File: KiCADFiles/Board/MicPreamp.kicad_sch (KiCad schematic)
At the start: 13 parts, among them U302B2 OPA2348, U6 THAT151xx08

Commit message: chose all components
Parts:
- removed C22: 3300u, ~, symbol PCM_SparkFun-Capacitor:C_Polarized_Small
- removed U302B2: OPA2348, symbol SuperAudioBoard-rescue:OPA2348
- added U10: OPA1655D, Package_SO:SOIC-8_3.9x4.9mm_P1.27mm, symbol Amplifier_Operational:OPA1655D
- C24, C39: value 470pF -> 470p; MPN (none) -> C0603C471J5GACTU
- C40: value 0.1uF -> 0.1u; MPN (none) -> CL10B104KB8NNNL
- R10: footprint (none) -> PCM_SparkFun-Resistor:R_0805_2012Metric; MPN (none) -> RC0805FR-074R7L
- R11, R17: footprint (none) -> PCM_SparkFun-Resistor:R_0805_2012Metric; MPN (none) -> ERA-6AEB102V
- R16, R7: footprint (none) -> PCM_SparkFun-Resistor:R_0805_2012Metric; MPN (none) -> ERA-6AEB3922V
- R6: value 10 -> 34; footprint ~ -> PCM_SparkFun-Resistor:R_0805_2012Metric; MPN (none) -> CRCW080534R0FKEA
- RV3: value RD_10k -> 5k; footprint (none) -> Potentiometer_THT:Potentiometer_Alps_RK163_Single_Horizontal; MPN (none) -> RV16AF-10-15K-C5K-3LA; now not fitted
- U6: value THAT151xx08 -> 1512S08-U; footprint (none) -> Package_SO:SOIC-8_5.3x5.3mm_P1.27mm; MPN (none) -> 1512S08-U
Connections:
- net +15V: now also U10.7 (V+)
- net GND: now also U10.4 (V-)
- net Rg-: now also RV3.3
- net at R6.1: now also U10.2 (-), U10.6
- net at R16.2, R7.1: now also U10.3 (+)
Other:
- moved on the sheet: R10

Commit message: replaced sw with relay, routed line amp section
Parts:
- added C22: 0.1u, PCM_SparkFun-Capacitor:C_0603_1608Metric, symbol PCM_SparkFun-Capacitor:0.1uF_0603_25V_20%
- C24, C39: footprint PCM_SparkFun-Capacitor:C_0603_1608Metric -> PCM_SparkFun-Capacitor:C_0805_2012Metric; MPN C0603C471J5GACTU -> 08053C471KAT2A
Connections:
- net +15V: now also C22.2
- net GND: now also C22.1
- net Rg-: now also RV3.2
- net at R10.2, RV3.1: no longer RV3.2
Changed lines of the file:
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@@
-	)
-	(junction
-		(at 160.02 114.3)
-		(diameter 0)
-		(color 0 0 0 0)
 	)
 	(junction
@@
 	)
 	(junction
+		(at 160.02 121.92)
+		(diameter 0)
+		(color 0 0 0 0)
+	)
+	(junction
 		(at 156.21 74.93)
+		(diameter 0)
+		(color 0 0 0 0)
+	)
+	(junction
+		(at 59.69 57.15)
 		(diameter 0)
 		(color 0 0 0 0)
@@
 	(wire
 		(pts
+			(xy 53.34 57.15) (xy 59.69 57.15)
+		)
+		(stroke
+			(width 0)
+			(type default)
+		)
+	)
+	(wire
+		(pts
 			(xy 199.39 72.39) (xy 198.12 72.39)
 		)
@@
 	(wire
 		(pts
+			(xy 163.83 121.92) (xy 160.02 121.92)
+		)
+		(stroke
+			(width 0)
+			(type default)
+		)
+	)
+	(wire
+		(pts
+			(xy 59.69 57.15) (xy 59.69 62.23)
+		)
+		(stroke
+			(width 0)
+			(type default)
+		)
+	)
+	(wire
+		(pts
 			(xy 45.72 72.39) (xy 54.61 72.39)
 		)
@@
 	(wire
 		(pts
-			(xy 59.69 57.15) (xy 59.69 62.23)
+			(xy 59.69 55.88) (xy 59.69 57.15)
 		)
 		(stroke
@@
 	(wire
 		(pts
+			(xy 163.83 118.11) (xy 163.83 121.92)
+		)
+		(stroke
+			(width 0)
+			(type default)
+		)
+	)
+	(wire
+		(pts
 			(xy 156.21 74.93) (xy 177.8 74.93)
 		)
@@
 	(wire
 		(pts
-			(xy 163.83 114.3) (xy 160.02 114.3)
-		)
-		(stroke
-			(width 0)
-			(type default)
-		)
-	)
-	(wire
-		(pts
 			(xy 160.02 113.03) (xy 160.02 114.3)
-		)
-		(stroke
-			(width 0)
-			(type default)
-		)
-	)
-	(wire
-		(pts
-			(xy 163.83 118.11) (xy 163.83 114.3)
 		)
 		(stroke
@@
 	)
 	(symbol
+		(lib_name "GND_13")
+		(lib_id "SuperAudioBoard-rescue:GND")
+		(at 53.34 62.23 0)
+		(unit 1)
+		(exclude_from_sim no)
+		(in_bom yes)
+		(on_board yes)
+		(dnp no)
+		(property "Reference" "#PWR067"
+			(at 53.34 62.23 0)
+			(effects
+				(font
+					(size 0.762 0.762)
+				)
+				(hide yes)
+			)
+		)
+		(property "Value" "GND"
+			(at 53.34 64.008 0)
+			(effects
+				(font
+					(size 0.762 0.762)
+				)
+				(hide yes)
+			)
+		)
+		(property "Footprint" ""
+			(at 53.34 62.23 0)
+			(effects
+				(font
+					(size 1.524 1.524)
+				)
+			)
+		)
+		(property "Datasheet" ""
+			(at 53.34 62.23 0)
+			(effects
+				(font
+					(size 1.524 1.524)
+				)
+			)
+		)
+		(property "Description" ""
+			(at 53.34 62.23 0)
+			(effects
+				(font
+					(size 1.27 1.27)
+				)
+			)
+		)
+		(pin "1"
+		)
+		(instances
+			(project "SuperAudioBoard"
+				(path "/01f65e03-4e05-4001-87b4-b3e88e4198ab/00000000-0000-0000-0000-00005438c479/cc56b259-b7b6-4889-861e-4cceeb5868cc"
+					(reference "#PWR067")
+					(unit 1)
+				)
+			)
+		)
+	)
+	(symbol
 		(lib_id "power:+15V")
 		(at 187.96 50.8 0)
@@
 	)
 	(symbol
+		(lib_id "PCM_SparkFun-Capacitor:0.1uF_0603_25V_20%")
+		(at 53.34 59.69 180)
+		(unit 1)
+		(exclude_from_sim no)
+		(in_bom yes)
+		(on_board yes)
+		(dnp no)
+		(property "Reference" "C22"
+			(at 47.498 59.9503 90)
+			(effects
+				(font
+					(size 1.27 1.27)
+				)
+			)
+		)
+		(property "Value" "0.1u"
+			(at 49.784 59.944 90)
+			(effects
+				(font
+					(size 1.27 1.27)
+				)
+			)
+		)
+		(property "Footprint" "PCM_SparkFun-Capacitor:C_0603_1608Metric"
+			(at 53.34 48.26 0)
+			(effects
+				(font
+					(size 1.27 1.27)
+				)
+				(hide yes)
+			)
+		)
+		(property "Datasheet" "https://cdn.sparkfun.com/assets/8/a/4/a/5/Kemet_Capacitor_Datasheet.pdf"
+			(at 53.34 45.72 0)
+			(effects
+				(font
+					(size 1.27 1.27)
+				)
+				(hide yes)
+			)
+		)
+		(property "Description" "Unpolarized capacitor"
+			(at 53.34 40.64 0)
+			(effects
+				(font
+					(size 1.27 1.27)
+				)
+				(hide yes)
+			)
+		)
+		(property "PROD_ID" "CAP-00810"
+			(at 53.34 43.18 0)
+			(effects
+				(font
+					(size 1.27 1.27)
+				)
+				(hide yes)
+			)
+		)
+		(property "Voltage" "25V"
+			(at 46.99 59.6837 90)
+			(effects
+				(font
+					(size 1.27 1.27)
+				)
+				(hide yes)
+			)
+		)
+		(property "Tolerance" "20%"
+			(at 49.53 59.6837 90)
+			(effects
+				(font
+					(size 1.27 1.27)
+				)
+				(hide yes)
+			)
+		)
+		(property "MPN" "CL10B104KB8NNNL"
+			(at 53.34 59.69 90)
+			(effects
+				(font
+					(size 1.27 1.27)
+				)
+				(hide yes)
+			)
+		)
+		(property "Tol" ""
+			(at 53.34 59.69 90)
+			(effects
+				(font
+					(size 1.27 1.27)
+				)
+				(hide yes)
+			)
+		)
+		(pin "2"
+		)
+		(pin "1"
+		)
+		(instances
+			(project "SuperAudioBoard"
+				(path "/01f65e03-4e05-4001-87b4-b3e88e4198ab/00000000-0000-0000-0000-00005438c479/cc56b259-b7b6-4889-861e-4cceeb5868cc"
+					(reference "C22")
+					(unit 1)
+				)
+			)
+		)
+	)
+	(symbol
 		(lib_id "Device:R_Small")
 		(at 156.21 72.39 180)
@@
 			)
 		)
-		(property "Footprint" "PCM_SparkFun-Capacitor:C_0603_1608Metric"
+		(property "Footprint" "PCM_SparkFun-Capacitor:C_0805_2012Metric"
 			(at 134.62 78.74 0)
 			(effects
@@
 			)
 		)
-		(property "MPN" "C0603C471J5GACTU"
+		(property "MPN" "08053C471KAT2A "
 			(at 134.62 67.31 0)
 			(effects
@@
 	(symbol
 		(lib_id "power:+15V")
-		(at 59.69 57.15 0)
+		(at 59.69 55.88 0)
 		(unit 1)
 		(exclude_from_sim no)
@@
 		(fields_autoplaced yes)
 		(property "Reference" "#PWR043"
-			(at 59.69 60.96 0)
+			(at 59.69 59.69 0)
 			(effects
 				(font
@@
 		)
 		(property "Value" "+15V"
-			(at 59.69 52.07 0)
+			(at 59.69 50.8 0)
 			(effects
 				(font
@@
 		)
 		(property "Footprint" ""
-			(at 59.69 57.15 0)
+			(at 59.69 55.88 0)
 			(effects
 				(font
@@
 		)
 		(property "Datasheet" ""
-			(at 59.69 57.15 0)
+			(at 59.69 55.88 0)
 			(effects
 				(font
@@
 		)
 		(property "Description" "Power symbol creates a global label with name \"+15V\""
-			(at 59.69 57.15 0)
+			(at 59.69 55.88 0)
 			(effects
 				(font
@@
 			)
 		)
-		(property "Footprint" "PCM_SparkFun-Capacitor:C_0603_1608Metric"
+		(property "Footprint" "PCM_SparkFun-Capacitor:C_0805_2012Metric"
 			(at 134.62 83.82 0)
 			(effects
@@
 			)
 		)
-		(property "MPN" "C0603C471J5GACTU"
+		(property "MPN" "08053C471KAT2A "
 			(at 134.62 72.39 0)
 			(effects

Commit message: improved layout further
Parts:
- removed RV3: 5k, Potentiometer_THT:Potentiometer_Alps_RK163_Single_Horizontal, symbol Device:R_Potentiometer
- added J10: 5k Log Pot, Connector_PinHeader_2.54mm:PinHeader_1x02_P2.54mm_Vertical, symbol Connector:Conn_01x02_Pin
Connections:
- net Rg-: now also J10.2 (Pin_2)
- net at R10.2: now also J10.1 (Pin_1)
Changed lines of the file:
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@@
-	)
-	(junction
-		(at 160.02 121.92)
-		(diameter 0)
-		(color 0 0 0 0)
 	)
 	(junction
@@
 	(wire
 		(pts
-			(xy 163.83 121.92) (xy 160.02 121.92)
-		)
-		(stroke
-			(width 0)
-			(type default)
-		)
-	)
-	(wire
-		(pts
 			(xy 59.69 57.15) (xy 59.69 62.23)
 		)
@@
 	(wire
 		(pts
-			(xy 163.83 118.11) (xy 163.83 121.92)
-		)
-		(stroke
-			(width 0)
-			(type default)
-		)
-	)
-	(wire
-		(pts
 			(xy 156.21 74.93) (xy 177.8 74.93)
 		)
@@
 	(wire
 		(pts
-			(xy 160.02 121.92) (xy 160.02 125.73)
+			(xy 160.02 119.38) (xy 160.02 125.73)
 		)
 		(stroke
@@
 	(wire
 		(pts
-			(xy 160.02 113.03) (xy 160.02 114.3)
+			(xy 160.02 113.03) (xy 160.02 116.84)
 		)
 		(stroke
@@
 	)
 	(symbol
-		(lib_id "Device:R_Potentiometer")
-		(at 160.02 118.11 0)
-		(unit 1)
-		(exclude_from_sim no)
-		(in_bom yes)
-		(on_board yes)
-		(dnp yes)
-		(fields_autoplaced yes)
-		(property "Reference" "RV3"
-			(at 157.48 116.8399 0)
-			(effects
-				(font
-					(size 1.27 1.27)
-				)
-				(justify right)
-			)
-		)
-		(property "Value" "5k"
-			(at 157.48 119.3799 0)
-			(effects
-				(font
-					(size 1.27 1.27)
-				)
-				(justify right)
-			)
-		)
-		(property "Footprint" "Potentiometer_THT:Potentiometer_Alps_RK163_Single_Horizontal"
-			(at 160.02 118.11 0)
-			(effects
-				(font
-					(size 1.27 1.27)
-				)
-				(hide yes)
-			)
-		)
-		(property "Datasheet" "~"
-			(at 160.02 118.11 0)
-			(effects
-				(font
-					(size 1.27 1.27)
-				)
-				(hide yes)
-			)
-		)
-		(property "Description" "Potentiometer"
-			(at 160.02 118.11 0)
-			(effects
-				(font
-					(size 1.27 1.27)
-				)
-				(hide yes)
-			)
-		)
-		(property "MPN" "RV16AF-10-15K-C5K-3LA "
-			(at 160.02 118.11 0)
-			(effects
-				(font
-					(size 1.27 1.27)
-				)
-				(hide yes)
-			)
-		)
-		(property "Tol" ""
-			(at 160.02 118.11 0)
-			(effects
-				(font
-					(size 1.27 1.27)
-				)
-				(hide yes)
-			)
-		)
-		(pin "3"
-		)
-		(pin "2"
-		)
-		(pin "1"
-		)
-		(instances
-			(project "SuperAudioBoard"
-				(path "/01f65e03-4e05-4001-87b4-b3e88e4198ab/00000000-0000-0000-0000-00005438c479/cc56b259-b7b6-4889-861e-4cceeb5868cc"
-					(reference "RV3")
-					(unit 1)
-				)
-			)
-		)
-	)
-	(symbol
 		(lib_id "Amplifier_Operational:OPA1655D")
 		(at 62.23 69.85 0)
@@
 					(unit 1)
 				)
+			)
+		)
+	)
+	(symbol
+		(lib_id "Connector:Conn_01x02_Pin")
+		(at 154.94 116.84 0)
+		(unit 1)
+		(exclude_from_sim no)
+		(in_bom yes)
+		(on_board yes)
+		(dnp no)
+		(fields_autoplaced yes)
+		(property "Reference" "J10"
+			(at 155.575 111.76 0)
+			(effects
+				(font
+					(size 1.27 1.27)
+				)
+			)
+		)
+		(property "Value" "5k Log Pot"
+			(at 155.575 114.3 0)
+			(effects
+				(font
+					(size 1.27 1.27)
+				)
+			)
+		)
+		(property "Footprint" "Connector_PinHeader_2.54mm:PinHeader_1x02_P2.54mm_Vertical"
+			(at 154.94 116.84 0)
+			(effects
+				(font
+					(size 1.27 1.27)
+				)
+				(hide yes)
+			)
+		)
+		(property "Datasheet" "~"
+			(at 154.94 116.84 0)
+			(effects
+				(font
+					(size 1.27 1.27)
+				)
+				(hide yes)
+			)
+		)
+		(property "Description" "Generic connector, single row, 01x02, script generated"
+			(at 154.94 116.84 0)
+			(effects
+				(font
+					(size 1.27 1.27)
+				)
+				(hide yes)
+			)
+		)
+		(property "MPN" "RV16AF-10-15K-C5K-3LA "
+			(at 154.94 116.84 0)
+			(effects
+				(font
+					(size 1.27 1.27)
+				)
+				(hide yes)
+			)
+		)
+		(pin "2"
+		)
+		(pin "1"
+		)
+		(instances
+			(project "SuperAudioBoard"
+				(path "/01f65e03-4e05-4001-87b4-b3e88e4198ab/00000000-0000-0000-0000-00005438c479/cc56b259-b7b6-4889-861e-4cceeb5868cc"
+					(reference "J10")
+					(unit 1)
+				)

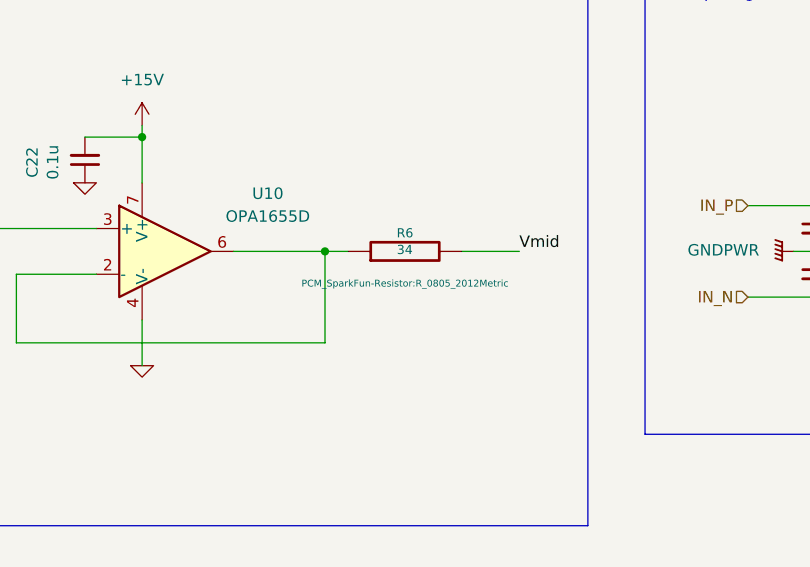
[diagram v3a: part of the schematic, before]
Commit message: finished layout, passed DRC
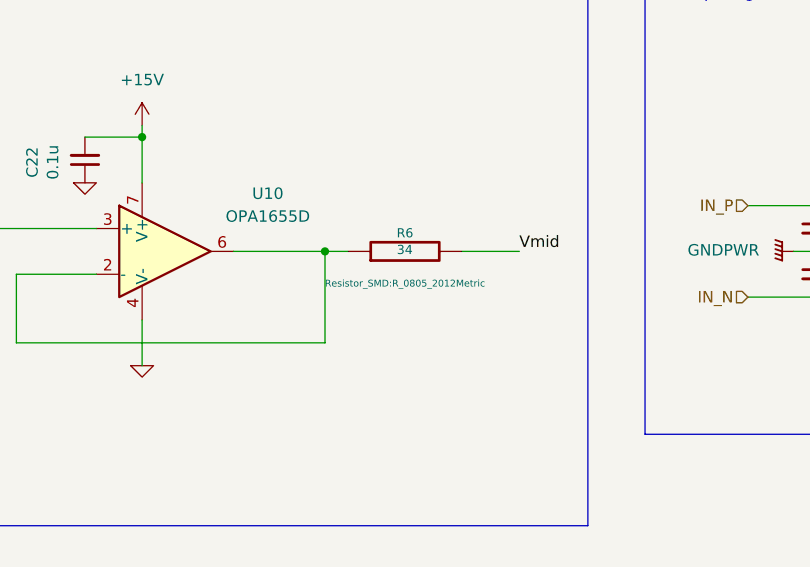
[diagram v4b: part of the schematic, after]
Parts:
- C22, C40: footprint PCM_SparkFun-Capacitor:C_0603_1608Metric -> Capacitor_SMD:C_0603_1608Metric_Pad1.08x0.95mm_HandSolder
- C24, C39: footprint PCM_SparkFun-Capacitor:C_0805_2012Metric -> Capacitor_SMD:C_0603_1608Metric_Pad1.08x0.95mm_HandSolder
- R10, R11, R16, R17, R6, R7: footprint PCM_SparkFun-Resistor:R_0805_2012Metric -> Resistor_SMD:R_0805_2012Metric
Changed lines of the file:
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@@
 			)
 		)
-		(property "Footprint" "PCM_SparkFun-Resistor:R_0805_2012Metric"
+		(property "Footprint" "Resistor_SMD:R_0805_2012Metric"
 			(at 88.9 73.406 90)
 			(effects
@@
 			)
 		)
-		(property "Footprint" "PCM_SparkFun-Resistor:R_0805_2012Metric"
+		(property "Footprint" "Resistor_SMD:R_0805_2012Metric"
 			(at 34.29 71.12 0)
 			(effects
@@
 			)
 		)
-		(property "Footprint" "PCM_SparkFun-Resistor:R_0805_2012Metric"
+		(property "Footprint" "Resistor_SMD:R_0805_2012Metric"
 			(at 156.21 67.31 0)
 			(effects
@@
 			)
 		)
-		(property "Footprint" "PCM_SparkFun-Resistor:R_0805_2012Metric"
+		(property "Footprint" "Resistor_SMD:R_0805_2012Metric"
 			(at 34.29 63.5 0)
 			(effects
@@
 			)
 		)
-		(property "Footprint" "PCM_SparkFun-Capacitor:C_0603_1608Metric"
+		(property "Footprint" "Capacitor_SMD:C_0603_1608Metric_Pad1.08x0.95mm_HandSolder"
 			(at 184.15 44.45 0)
 			(effects
@@
 			)
 		)
-		(property "Footprint" "PCM_SparkFun-Capacitor:C_0603_1608Metric"
+		(property "Footprint" "Capacitor_SMD:C_0603_1608Metric_Pad1.08x0.95mm_HandSolder"
 			(at 53.34 48.26 0)
 			(effects
@@
 			)
 		)
-		(property "Footprint" "PCM_SparkFun-Resistor:R_0805_2012Metric"
+		(property "Footprint" "Resistor_SMD:R_0805_2012Metric"
 			(at 156.21 72.39 0)
 			(effects
@@
 			)
 		)
-		(property "Footprint" "PCM_SparkFun-Capacitor:C_0805_2012Metric"
+		(property "Footprint" "Capacitor_SMD:C_0603_1608Metric_Pad1.08x0.95mm_HandSolder"
 			(at 134.62 78.74 0)
 			(effects
@@
 			)
 		)
-		(property "Footprint" "PCM_SparkFun-Resistor:R_0805_2012Metric"
+		(property "Footprint" "Resistor_SMD:R_0805_2012Metric"
 			(at 160.02 110.49 0)
 			(effects
@@
 			)
 		)
-		(property "Footprint" "PCM_SparkFun-Capacitor:C_0805_2012Metric"
+		(property "Footprint" "Capacitor_SMD:C_0603_1608Metric_Pad1.08x0.95mm_HandSolder"
 			(at 134.62 83.82 0)
 			(effects
